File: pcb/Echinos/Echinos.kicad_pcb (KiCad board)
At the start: 4 copper layers, 143.8 x 117.6 mm, 136 parts, among them J1 USB_C_Receptacle_USB2.0, J2 FPC (PCB), J206 Conn_01x06_Pin, J207 FPC (module), J209 Joystick, J3 TagConnect_6pins, J4 FPC_VIK, J5 SATA-7p, SW1 SW_Push, SW101 RotaryEncoder_Switch, SW102 SW_Push, SW103 SW_Push, SW105 SW_Push, SW106 SW_Push, SW107 SW_Push, SW108 SW_Push, SW109 SW_Push, SW110 SW_Push, SW111 SW_Push, SW112 SW_Push, SW113 SW_Push, SW114 SW_Push, SW115 SW_Push, SW116 SW_Push, SW117 SW_Push, SW118 SW_Push, SW119 SW_Push, SW120 SW_Push, SW2 SW_Push, U1 RP2040, U2 XC6210B332MR-G, U205 PMW3360DM-T2QU, U206 XC6206P202MR-G, U3 ESD7L5.0DT5G-N, U4 W25Q128JVS, U7 SRV05-4, X1 ASE-12MHz

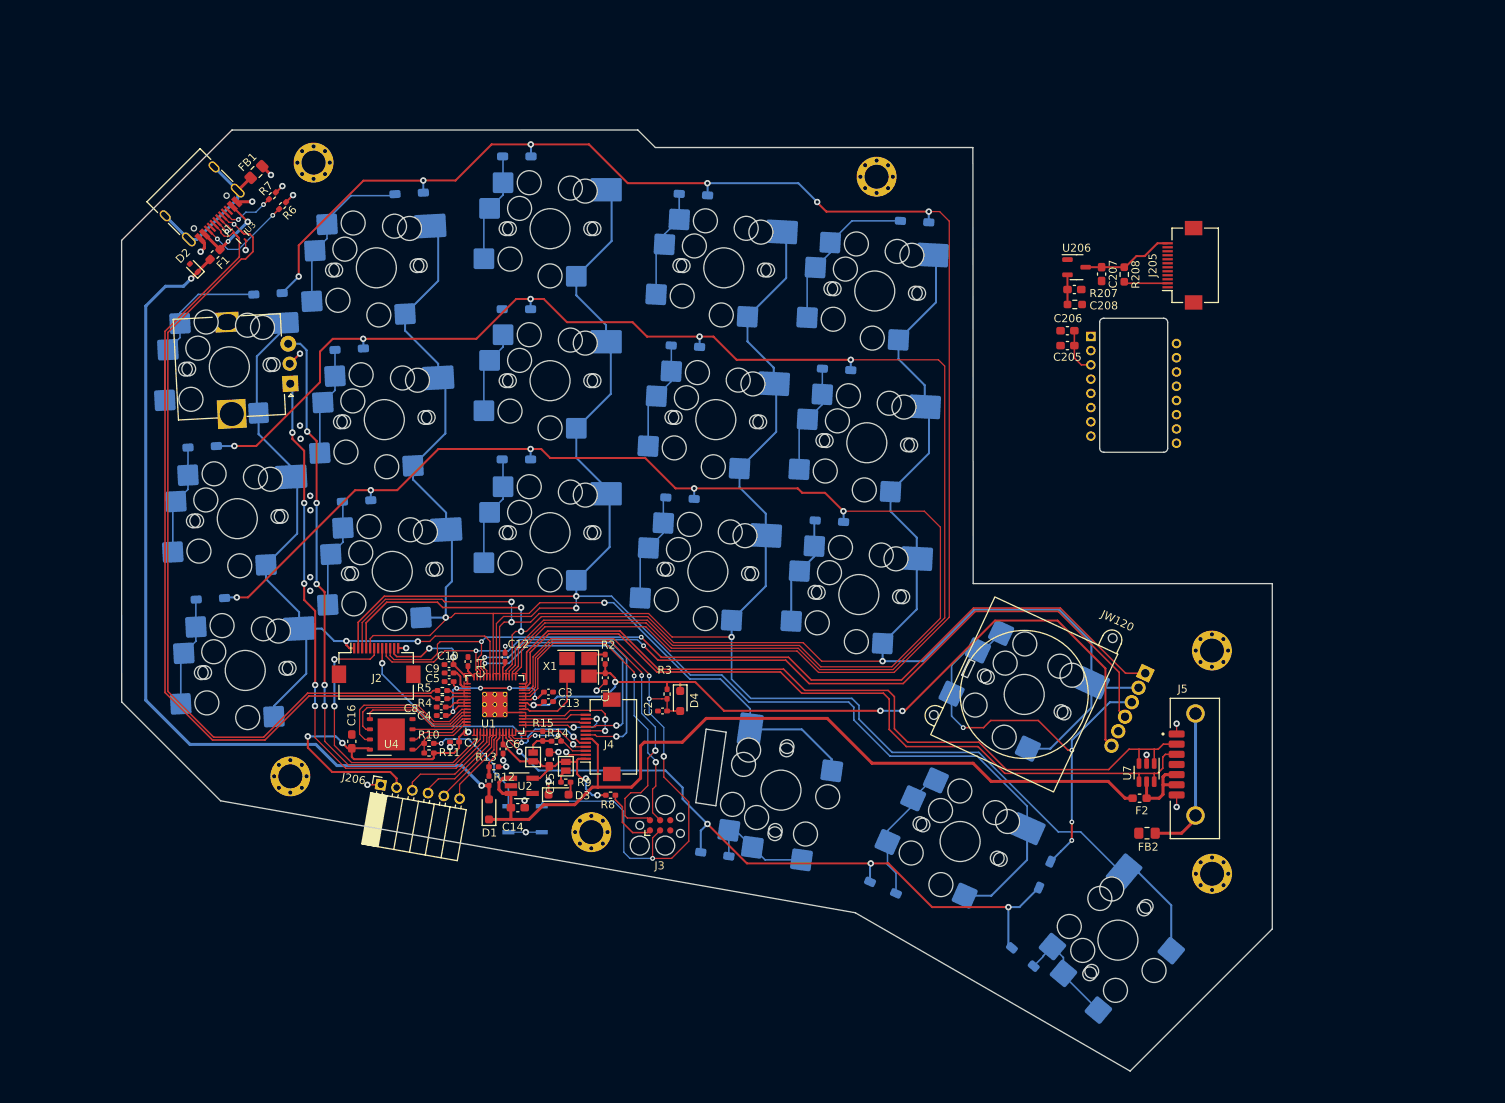
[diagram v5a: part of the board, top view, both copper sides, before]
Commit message: ♻️ [PCB] - Now using the same ESD protection on both SATA and USB. Add ground fill and earth fill using ferrite bead as gate between both.
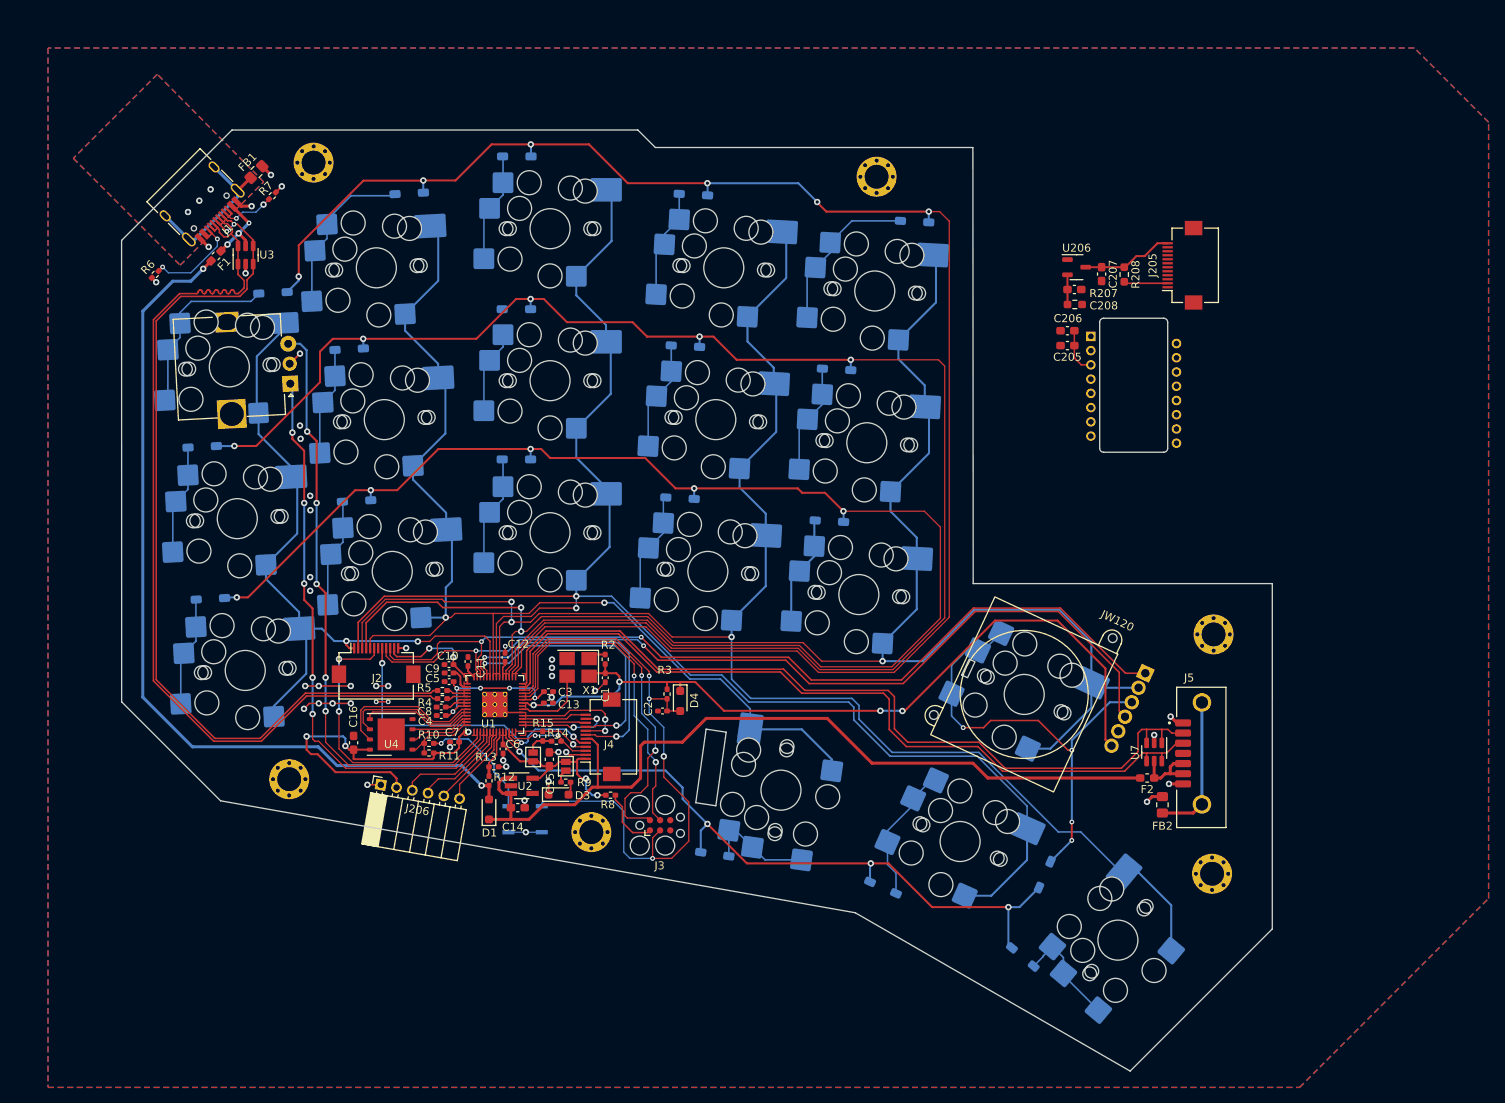
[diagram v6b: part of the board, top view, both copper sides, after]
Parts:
- removed D2: TPD1E10B06-Q1, Diode_SMD:D_SOD-523
- U3: value ESD7L5.0DT5G-N -> SRV05-4; footprint Echinos:D_TVS_SOT-723 -> Package_TO_SOT_SMD:SOT-23-6
- moved R6 18.1 mm to (80.7, 85.2), turned to -135 degrees
- moved FB2 4.04 mm to (206.6, 151.5), turned to 90 degrees
- moved U7 2.74 mm to (205.5, 144.9)
- moved F2 2.70 mm to (204.7, 148.2)
- moved U3 2.28 mm to (92.0, 82.8), turned to 90 degrees
- moved H6 2.03 mm to (212.9, 130.2)
- moved J5 1.60 mm to (211.5, 145.6)
- moved D101 0.64 mm to (95.4, 87.5)
- moved H3 0.38 mm to (97.4, 148.3)
- moved C16 0.29 mm to (105.5, 143.8)
- moved F1 0.22 mm to (88.2, 82.9)
- moved C13 0.18 mm to (129.8, 138.8)
- moved C3 0.06 mm to (129.8, 137.3)
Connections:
- U3 pad 1: /Left Side/USB_D- -> /Left Side/USB_D+
- U3 pad 2: /Left Side/USB_D+ -> GND
- U3 pad 3: GND -> /Left Side/USB_D-
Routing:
- net GND: track 35.1 -> 53.5 mm, vias 28 -> 44
- net /Left Side/USB_D+: track 106.7 -> 115.0 mm
- net /Left Side/USB_D-: track 106.7 -> 113.1 mm
- net RX: track 101.2 -> 104.1 mm
- net rgb: track 37.0 -> 39.7 mm
- net +3.3V: track 192.2 -> 193.7 mm
- net VBUS_split: track 10.0 -> 8.56 mm
- net row5: track 37.6 -> 36.7 mm
- net Net-(FB2-Pad1): track 19.0 -> 18.1 mm
- net /Left Side/RP2040_Left/SWCLK: track 40.6 -> 41.4 mm
- net adc_2: track 36.8 -> 37.6 mm
- net /Left Side/RP2040_Left/QSPI_SD3: track 19.8 -> 19.0 mm
- net adc_3: track 33.5 -> 34.3 mm
- net /Left Side/Matrix_Left/encoder_out: track 21.9 -> 22.6 mm
- net /Left Side/RP2040_Left/SWDIO: track 45.7 -> 46.3 mm
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- added copper zone on B.Cu, net Earth
- added copper zone on F.Cu, net Earth
- added copper zone on In1.Cu, net Earth
- added copper zone on In2.Cu, net Earth
- added copper zone on B.Cu, net GND
- added copper zone on F.Cu, net GND
- added copper zone on In1.Cu, net GND
- added copper zone on In2.Cu, net GND
